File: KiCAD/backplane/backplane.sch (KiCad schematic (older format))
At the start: 29 parts, among them CON1 AVR-JTAG-10, P1 CONN_02X04, P10 CONN_02X04, P11 CONN_01X09, P12 CONN_02X04, P13 CONN_01X09, P14 CONN_01X10, P15 CONN_01X10, P16 CONN_02X04, P17 CONN_02X04, P18 CONN_02X04, P19 CONN_01X09, P2 CONN_01X17, P20 CONN_01X04, P21 CONN_01X02, P22 CONN_01X02, P23 CONN_01X02, P3 CONN_01X17, P4 CONN_01X04, P5 CONN_01X09, P6 CONN_02X04, P7 CONN_01X10, P8 CONN_01X10, P9 CONN_02X04, U1 ARDUINO_MICRO

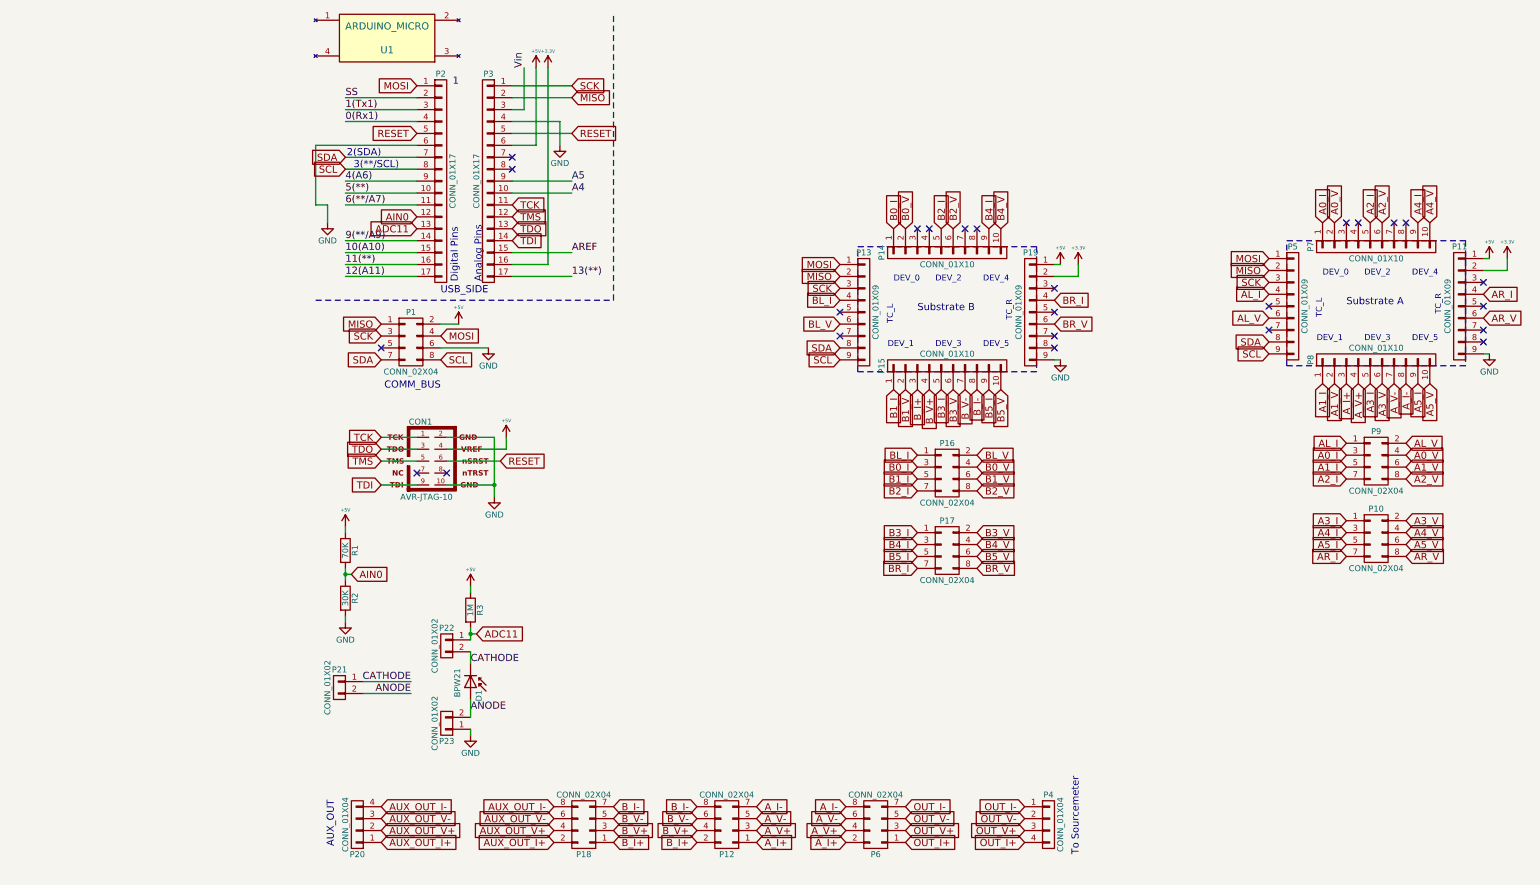
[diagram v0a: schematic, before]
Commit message: switch adapter board mounting
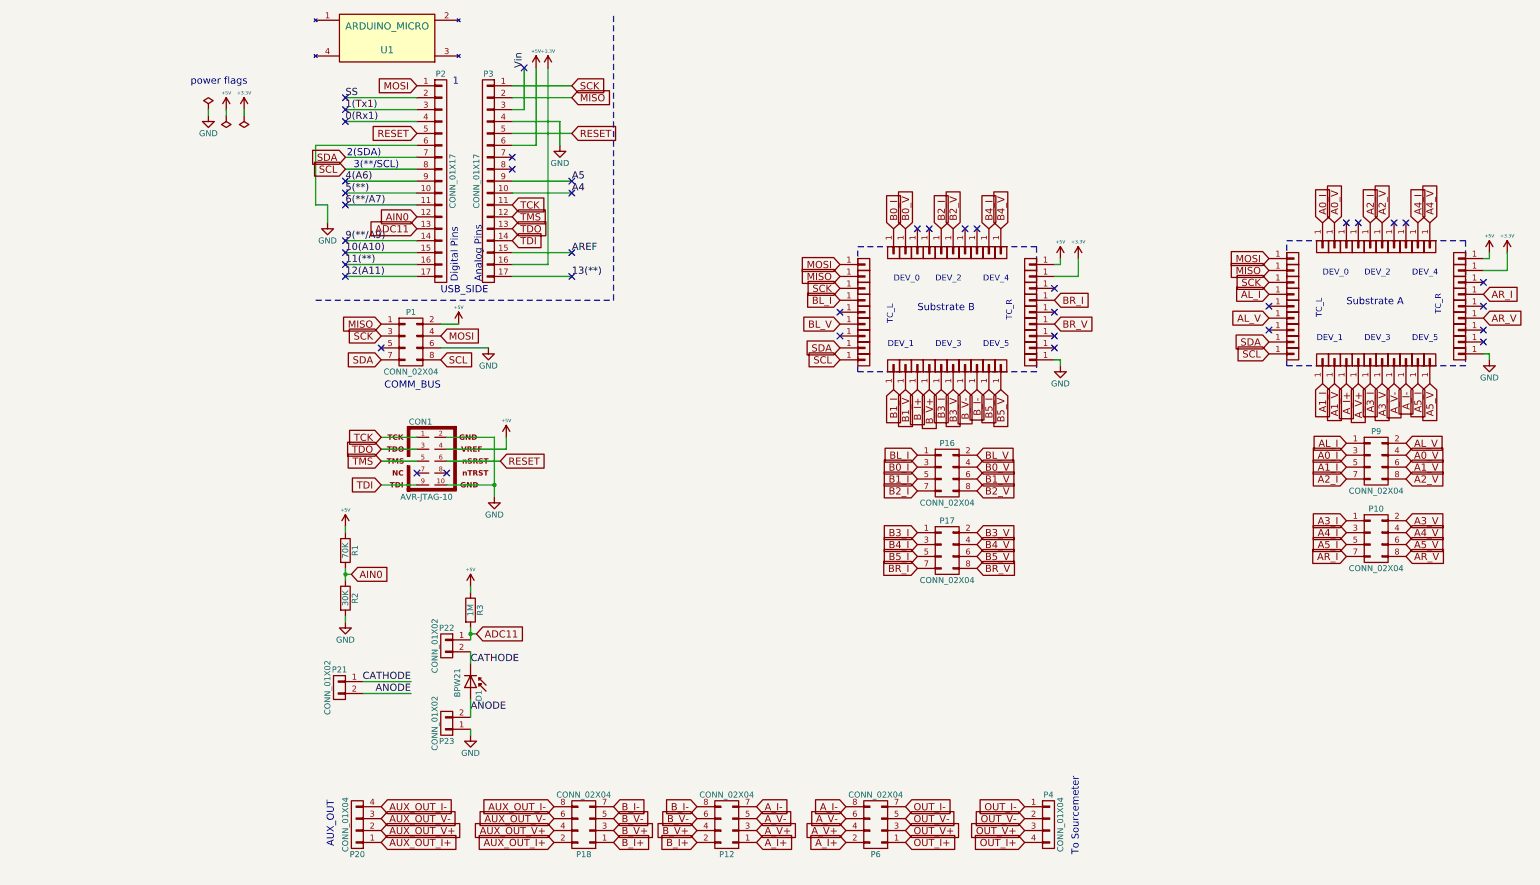
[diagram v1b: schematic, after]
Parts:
- removed P11, P13, P19, P5: CONN_01X09, Socket_Strips:Socket_Strip_Straight_1x09, symbol CONN_01X09
- removed P14, P15, P7, P8: CONN_01X10, Socket_Strips:Socket_Strip_Straight_1x10, symbol CONN_01X10
- added P11, P13, P14, P15, P19, P24, P25, P26, P27, P28, P29, P30, P31, P32, P33, P34, P35, P36, P37, P38, P39, P40, P41, P42, P43, P44, P45, P46, P47, P48, P49, P5, P50, P51, P52, P53, P54, P55, P56, P57, P58, P59, P60, P61, P62, P63, P64, P65, P66, P67, P68, P69, P7, P70, P71, P72, P73, P74, P75, P76, P77, P78, P79, P8, P80, P81, P82, P83, P84, P85, P86, P87, P88, P89, P90, P91: CONN_01X01, myparts:4994-0-15-15-11-27-10-0, symbol CONN_01X01
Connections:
- net +3V3: now also P33.1 (P1), P51.1 (P1)
- net +5V: now also P13.1 (P1), P50.1 (P1)
- net A0_I: now also P72.1 (P1)
- net A0_V: now also P74.1 (P1)
- net A1_I: now also P73.1 (P1)
- net A1_V: now also P75.1 (P1)
- net A2_I: now also P80.1 (P1)
- net A2_V: now also P82.1 (P1)
- net A3_I: now also P81.1 (P1)
- net A3_V: now also P83.1 (P1)
- net A4_I: now also P88.1 (P1)
- net A4_V: now also P90.1 (P1)
- net A5_I: now also P89.1 (P1)
- net A5_V: now also P91.1 (P1)
- net AL_I: now also P44.1 (P1)
- net AL_V: now also P46.1 (P1)
- net AR_I: now also P53.1 (P1)
- net AR_V: now also P55.1 (P1)
- net A_I+: now also P77.1 (P1)
- net A_I-: now also P87.1 (P1)
- net A_V+: now also P79.1 (P1)
- net A_V-: now also P85.1 (P1)
- net B0_I: now also P5.1 (P1)
- net B0_V: now also P8.1 (P1)
- net B1_I: now also P7.1 (P1)
- net B1_V: now also P11.1 (P1)
- net B2_I: now also P60.1 (P1)
- net B2_V: now also P62.1 (P1)
- net B3_I: now also P61.1 (P1)
- net B3_V: now also P63.1 (P1)
- net B4_I: now also P68.1 (P1)
- net B4_V: now also P70.1 (P1)
- net B5_I: now also P69.1 (P1)
- net B5_V: now also P71.1 (P1)
- net BL_I: now also P27.1 (P1)
- net BL_V: now also P29.1 (P1)
- net BR_I: now also P35.1 (P1)
- net BR_V: now also P37.1 (P1)
- net B_I+: now also P15.1 (P1)
- net B_I-: now also P67.1 (P1)
- net B_V+: now also P59.1 (P1)
- net B_V-: now also P65.1 (P1)
- net GND: now also P40.1 (P1), P58.1 (P1)
- net MISO: now also P25.1 (P1), P42.1 (P1)
- net MOSI: now also P24.1 (P1), P41.1 (P1)
- net SCK: now also P26.1 (P1), P43.1 (P1)
- net SCL: now also P32.1 (P1), P49.1 (P1)
- net SDA: now also P31.1 (P1), P48.1 (P1)
- no-connect marks 25 -> 40
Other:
- note added: "power flags"

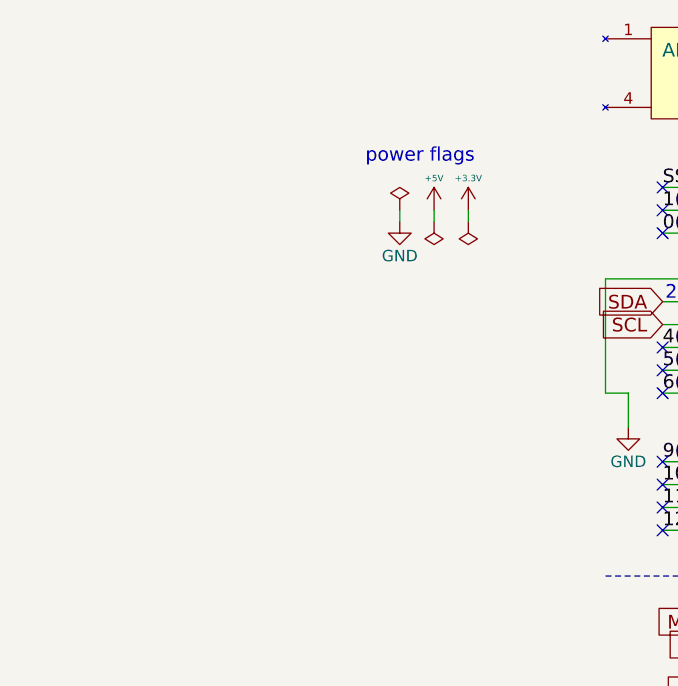
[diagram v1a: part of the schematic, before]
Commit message: properly link mounting holes to schematic
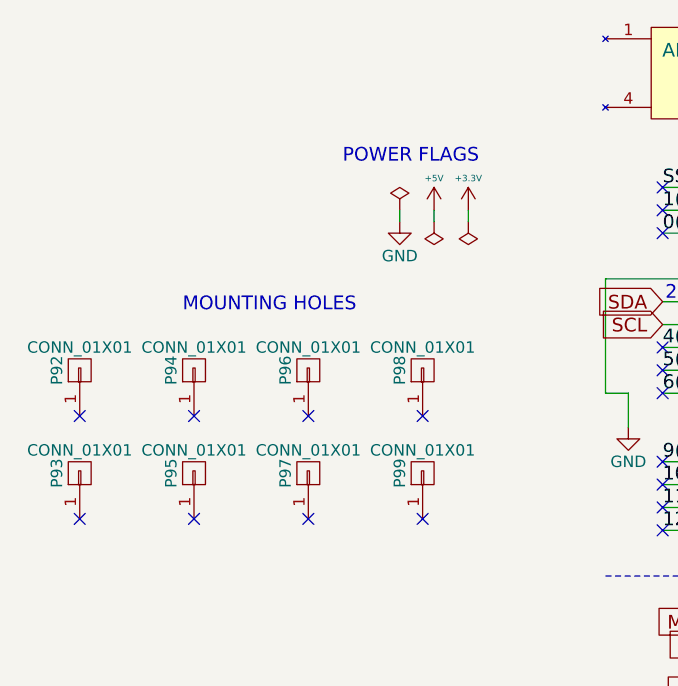
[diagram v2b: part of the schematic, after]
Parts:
- added P92, P96, P97, P98, P99: CONN_01X01, Mounting_Holes:MountingHole_3.2mm_M3_Pad, symbol CONN_01X01
- added P93, P95: CONN_01X01, Mounting_Holes:MountingHole_6mm, symbol CONN_01X01
- added P94: CONN_01X01, Mounting_Holes:MountingHole_4.3mm_M4, symbol CONN_01X01
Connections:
- no-connect marks 40 -> 48
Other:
- note added: "MOUNTING HOLES"
- note added: "POWER FLAGS"
- note removed: "power flags"
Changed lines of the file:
@@
 Wire Wire Line
 	-100 1300 -100 1350
-Text Notes -550 1100 0    60   ~ 0
-power flags
+Text Notes -650 1100 0    60   ~ 0
+POWER FLAGS
 $Comp
 L CONN_01X01 P13
@@
 	0    1    -1   0
 $EndComp
+$Comp
+L CONN_01X01 P96
+U 1 1 587F4EA3
+P -800 2000
+F 0 "P96" H -800 2100 50  0000 C CNN
+F 1 "CONN_01X01" V -700 2000 50  0000 C CNN
+F 2 "Mounting_Holes:MountingHole_3.2mm_M3_Pad" H -800 2000 50  0001 C CNN
+F 3 "" H -800 2000 50  0000 C CNN
+	1    -800 2000
+	0    -1   -1   0
+$EndComp
+$Comp
+L CONN_01X01 P94
+U 1 1 587F4FEE
+P -1300 2000
+F 0 "P94" H -1300 2100 50  0000 C CNN
+F 1 "CONN_01X01" V -1200 2000 50  0000 C CNN
+F 2 "Mounting_Holes:MountingHole_4.3mm_M4" H -1300 2000 50  0001 C CNN
+F 3 "" H -1300 2000 50  0000 C CNN
+	1    -1300 2000
+	0    -1   -1   0
+$EndComp
+$Comp
+L CONN_01X01 P92
+U 1 1 587F506F
+P -1800 2000
+F 0 "P92" H -1800 2100 50  0000 C CNN
+F 1 "CONN_01X01" V -1700 2000 50  0000 C CNN
+F 2 "Mounting_Holes:MountingHole_3.2mm_M3_Pad" H -1800 2000 50  0001 C CNN
+F 3 "" H -1800 2000 50  0000 C CNN
+	1    -1800 2000
+	0    -1   -1   0
+$EndComp
+$Comp
+L CONN_01X01 P97
+U 1 1 587F50F3
+P -800 2450
+F 0 "P97" H -800 2550 50  0000 C CNN
+F 1 "CONN_01X01" V -700 2450 50  0000 C CNN
+F 2 "Mounting_Holes:MountingHole_3.2mm_M3_Pad" H -800 2450 50  0001 C CNN
+F 3 "" H -800 2450 50  0000 C CNN
+	1    -800 2450
+	0    -1   -1   0
+$EndComp
+$Comp
+L CONN_01X01 P99
+U 1 1 587F515E
+P -300 2450
+F 0 "P99" H -300 2550 50  0000 C CNN
+F 1 "CONN_01X01" V -200 2450 50  0000 C CNN
+F 2 "Mounting_Holes:MountingHole_3.2mm_M3_Pad" H -300 2450 50  0001 C CNN
+F 3 "" H -300 2450 50  0000 C CNN
+	1    -300 2450
+	0    -1   -1   0
+$EndComp
+$Comp
+L CONN_01X01 P98
+U 1 1 587F51CE
+P -300 2000
+F 0 "P98" H -300 2100 50  0000 C CNN
+F 1 "CONN_01X01" V -200 2000 50  0000 C CNN
+F 2 "Mounting_Holes:MountingHole_3.2mm_M3_Pad" H -300 2000 50  0001 C CNN
+F 3 "" H -300 2000 50  0000 C CNN
+	1    -300 2000
+	0    -1   -1   0
+$EndComp
+$Comp
+L CONN_01X01 P95
+U 1 1 587F55C2
+P -1300 2450
+F 0 "P95" H -1300 2550 50  0000 C CNN
+F 1 "CONN_01X01" V -1200 2450 50  0000 C CNN
+F 2 "Mounting_Holes:MountingHole_6mm" H -1300 2450 50  0001 C CNN
+F 3 "" H -1300 2450 50  0000 C CNN
+	1    -1300 2450
+	0    -1   -1   0
+$EndComp
+$Comp
+L CONN_01X01 P93
+U 1 1 587F563E
+P -1800 2450
+F 0 "P93" H -1800 2550 50  0000 C CNN
+F 1 "CONN_01X01" V -1700 2450 50  0000 C CNN
+F 2 "Mounting_Holes:MountingHole_6mm" H -1800 2450 50  0001 C CNN
+F 3 "" H -1800 2450 50  0000 C CNN
+	1    -1800 2450
+	0    -1   -1   0
+$EndComp
+NoConn ~ -1800 2200
+NoConn ~ -1300 2200
+NoConn ~ -800 2200
+NoConn ~ -300 2200
+NoConn ~ -300 2650
+NoConn ~ -800 2650
+NoConn ~ -1300 2650
+NoConn ~ -1800 2650
+Text Notes -1350 1750 0    60   ~ 0
+MOUNTING HOLES
 $EndSCHEMATC

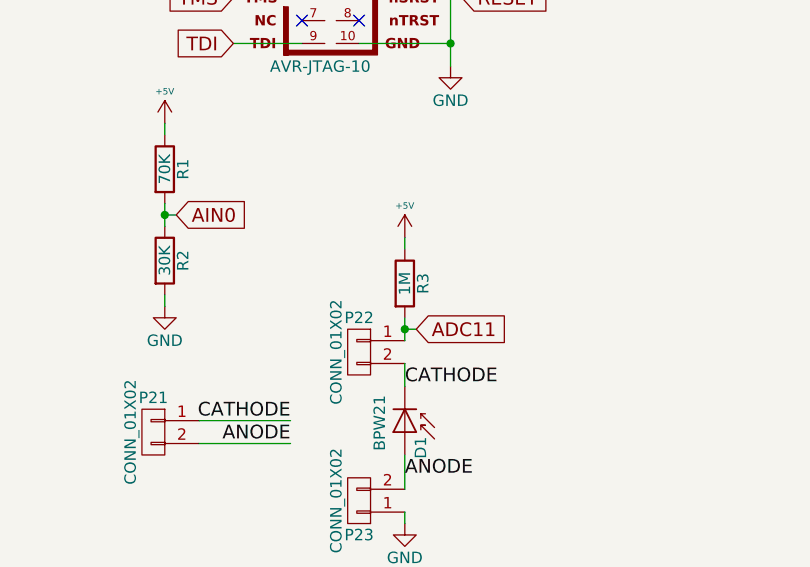
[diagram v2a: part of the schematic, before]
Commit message: fix diode sense resistor
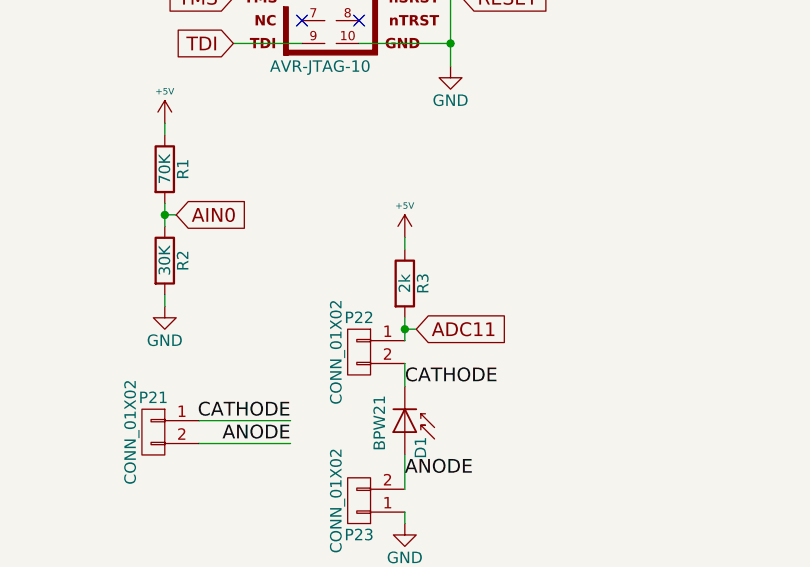
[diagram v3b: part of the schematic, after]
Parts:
- R3: value 1M -> 2k
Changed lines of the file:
@@
 P 1800 5500
 F 0 "R3" V 1880 5500 50  0000 C CNN
-F 1 "1M" V 1800 5500 50  0000 C CNN
+F 1 "2k" V 1800 5500 50  0000 C CNN
 F 2 "Resistors_SMD:R_0805_HandSoldering" V 1730 5500 50  0001 C CNN
 F 3 "" H 1800 5500 50  0000 C CNN

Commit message: fix up some hardware bugs
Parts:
- added R4, R5: 10K, Resistors_SMD:R_0805_HandSoldering, symbol R
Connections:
- net +5V: now also R4.1, R5.1
- net SCL: now also R5.2
- net SDA: now also R4.2
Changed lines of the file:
@@
 Text Notes -1350 1750 0    60   ~ 0
 MOUNTING HOLES
+Text GLabel 2500 3200 0    60   Input ~ 0
+SDA
+Text GLabel 2500 3400 0    60   Input ~ 0
+SCL
+$Comp
+L +5V #PWR025
+U 1 1 58A871E2
+P 2900 3150
+F 0 "#PWR025" H 2900 3000 50  0001 C CNN
+F 1 "+5V" H 2900 3290 28  0000 C CNN
+F 2 "" H 2900 3150 50  0000 C CNN
+F 3 "" H 2900 3150 50  0000 C CNN
+	1    2900 3150
+	1    0    0    -1
+$EndComp
+$Comp
+L R R4
+U 1 1 58A87244
+P 2700 3200
+F 0 "R4" V 2780 3200 50  0000 C CNN
+F 1 "10K" V 2700 3200 50  0000 C CNN
+F 2 "Resistors_SMD:R_0805_HandSoldering" V 2630 3200 50  0001 C CNN
+F 3 "" H 2700 3200 50  0000 C CNN
+	1    2700 3200
+	0    1    1    0
+$EndComp
+$Comp
+L R R5
+U 1 1 58A87414
+P 2700 3400
+F 0 "R5" V 2780 3400 50  0000 C CNN
+F 1 "10K" V 2700 3400 50  0000 C CNN
+F 2 "Resistors_SMD:R_0805_HandSoldering" V 2630 3400 50  0001 C CNN
+F 3 "" H 2700 3400 50  0000 C CNN
+	1    2700 3400
+	0    1    1    0
+$EndComp
+Wire Wire Line
+	2500 3200 2550 3200
+Wire Wire Line
+	2500 3400 2550 3400
+Wire Wire Line
+	2900 3150 2900 3400
+Wire Wire Line
+	2900 3200 2850 3200
+Wire Wire Line
+	2900 3400 2850 3400
+Connection ~ 2900 3200
 $EndSCHEMATC
